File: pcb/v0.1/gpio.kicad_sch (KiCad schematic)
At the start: 36 parts, among them J7 ComputeModule5-CM5_connector, J8 Micro_SD_molex, J9 AudioJack3, SW1 SW_Push_45deg, U4 PCM5102A, U5 RT9742GGJ5, U6 RT9742GGJ5

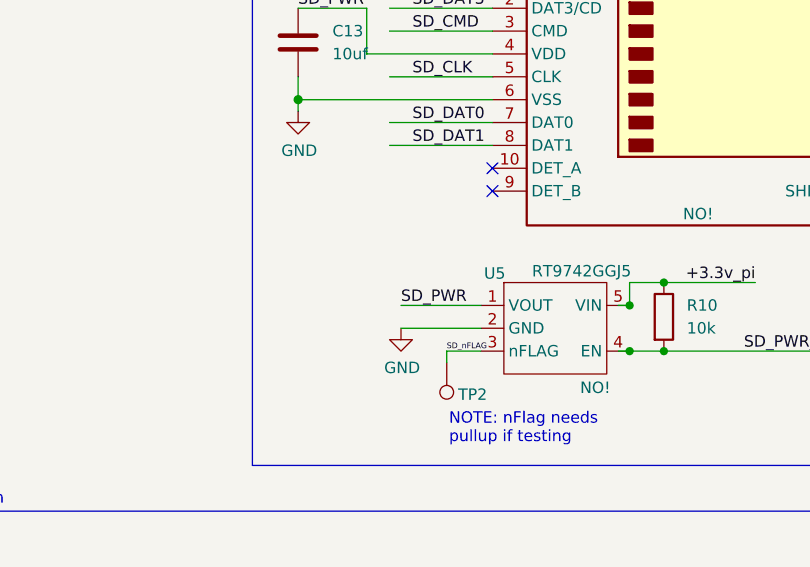
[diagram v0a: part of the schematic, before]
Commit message: Add test points
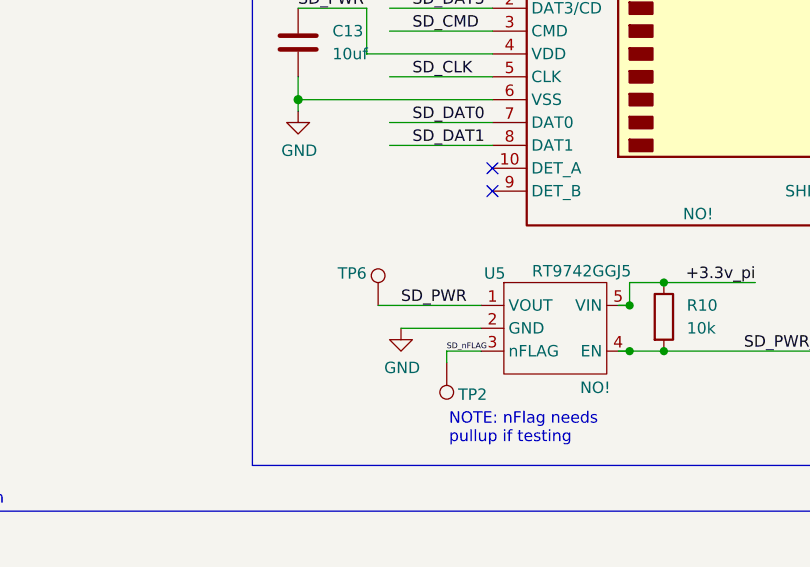
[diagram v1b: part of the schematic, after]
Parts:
- added TP6: TestPoint, symbol Connector:TestPoint
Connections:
- net SD_PWR: now also TP6.1
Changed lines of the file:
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@@
 	(wire
 		(pts
+			(xy 341.63 106.68) (xy 353.06 106.68)
+		)
+		(stroke
+			(width 0)
+			(type default)
+		)
+	)
+	(wire
+		(pts
 			(xy 347.98 203.2) (xy 356.87 203.2)
 		)
@@
 	(wire
 		(pts
-			(xy 353.06 106.68) (xy 344.17 106.68)
-		)
-		(stroke
-			(width 0)
-			(type solid)
-		)
-	)
-	(wire
-		(pts
 			(xy 304.8 228.6) (xy 304.8 229.87)
 		)
@@
 					(unit 1)
 				)
+			)
+		)
+	)
+	(symbol
+		(lib_id "Connector:TestPoint")
+		(at 341.63 106.68 0)
+		(unit 1)
+		(body_style 1)
+		(exclude_from_sim no)
+		(in_bom yes)
+		(on_board yes)
+		(in_pos_files yes)
+		(dnp no)
+		(property "Reference" "TP6"
+			(at 340.36 103.124 0)
+			(show_name no)
+			(do_not_autoplace no)
+			(effects
+				(font
+					(size 1.27 1.27)
+				)
+				(justify right)
+			)
+		)
+		(property "Value" "TestPoint"
+			(at 339.09 102.1081 0)
+			(hide yes)
+			(show_name no)
+			(do_not_autoplace no)
+			(effects
+				(font
+					(size 1.27 1.27)
+				)
+				(justify right)
+			)
+		)
+		(property "Footprint" ""
+			(at 346.71 106.68 0)
+			(hide yes)
+			(show_name no)
+			(do_not_autoplace no)
+			(effects
+				(font
+					(size 1.27 1.27)
+				)
+			)
+		)
+		(property "Datasheet" ""
+			(at 346.71 106.68 0)
+			(hide yes)
+			(show_name no)
+			(do_not_autoplace no)
+			(effects
+				(font
+					(size 1.27 1.27)
+				)
+			)
+		)
+		(property "Description" "test point"
+			(at 341.63 106.68 0)
+			(hide yes)
+			(show_name no)
+			(do_not_autoplace no)
+			(effects
+				(font
+					(size 1.27 1.27)
+				)
+			)
+		)
+		(pin "1"
+		)
+		(instances
+			(project "mainboard"
+				(path "/5b8aa782-5c3d-43e7-a869-3bd000015f52/5721f8f0-0440-46b6-aeef-45d87b753dcc"
+					(reference "TP6")
+					(unit 1)
+				)

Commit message: Make the ERC happy
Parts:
- removed R11: 0R, Resistor_SMD:R_0603_1608Metric, symbol TH-1-CC:R_0Ω
- added R31: 0R, Resistor_SMD:R_0603_1608Metric, symbol TH-1-CC:R_0Ω
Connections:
- net +3v3_PI: now also R31.1
- net GPIO_VREF: now also R31.2
- net SD_CMD: now also J7.62 (SD_CMD)
- no-connect marks 36 -> 35
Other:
- note removed: "GPIO Voltage select"
- moved on the sheet: FB1, FB2, SW1

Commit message: Small corrections
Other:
- moved on the sheet: C23, J7A, R31
